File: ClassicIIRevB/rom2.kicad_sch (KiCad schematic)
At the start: 2 parts

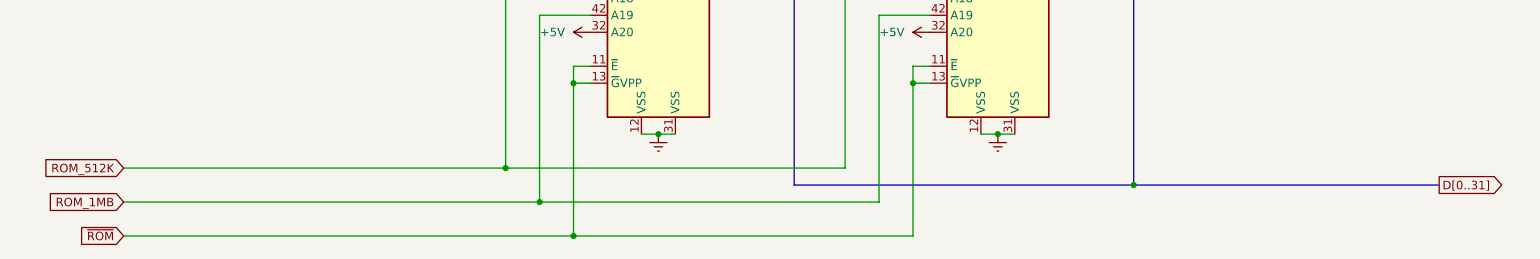
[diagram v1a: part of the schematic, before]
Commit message: Switch to some "official" net names
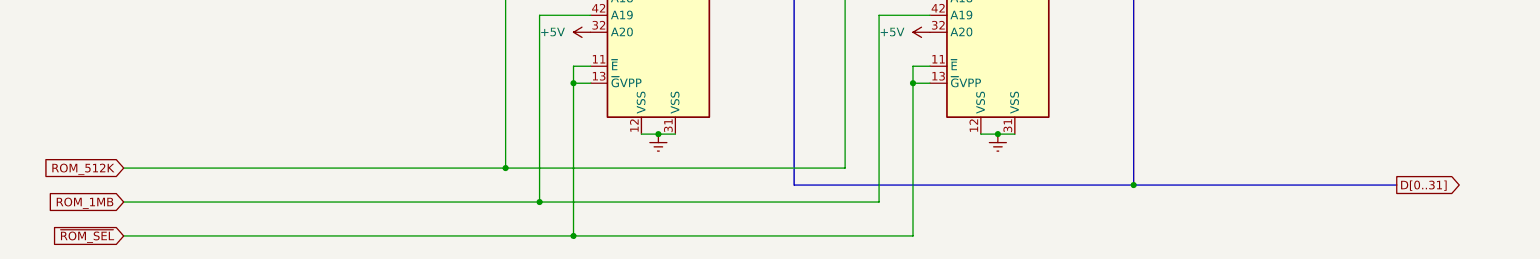
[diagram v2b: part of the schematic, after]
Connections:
- net ~{ROM} renamed ~{ROM_SEL}
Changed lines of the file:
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@@
 	(bus
 		(pts
-			(xy 195.58 139.7) (xy 241.3 139.7)
+			(xy 195.58 139.7) (xy 234.95 139.7)
 		)
 		(stroke
@@
 	(global_label "D[0..31]"
 		(shape output)
-		(at 241.3 139.7 0)
+		(at 234.95 139.7 0)
 		(fields_autoplaced yes)
 		(effects
@@
 		)
 		(property "Intersheetrefs" "${INTERSHEET_REFS}"
-			(at 252.0867 139.7 0)
+			(at 245.7367 139.7 0)
 			(effects
 				(font
@@
 		)
 	)
-	(global_label "~{ROM}"
+	(global_label "~{ROM_SEL}"
 		(shape input)
 		(at 44.45 147.32 180)
@@
 		)
 		(property "Intersheetrefs" "${INTERSHEET_REFS}"
-			(at 34.9334 147.32 0)
+			(at 33.0587 147.32 0)
 			(effects
 				(font

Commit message: update exports
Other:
- title: Macintosh Classic II Revision B -> Macintosh Classic II (Later Revision)
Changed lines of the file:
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@@
 	(paper "USLetter")
 	(title_block
-		(title "Macintosh Classic II Revision B")
-		(date "2025-06-04")
+		(title "Macintosh Classic II (Later Revision)")
+		(date "2025-06-16")
 		(company "Apple Computer")
 		(comment 1 "drawn by Bradley Bell")

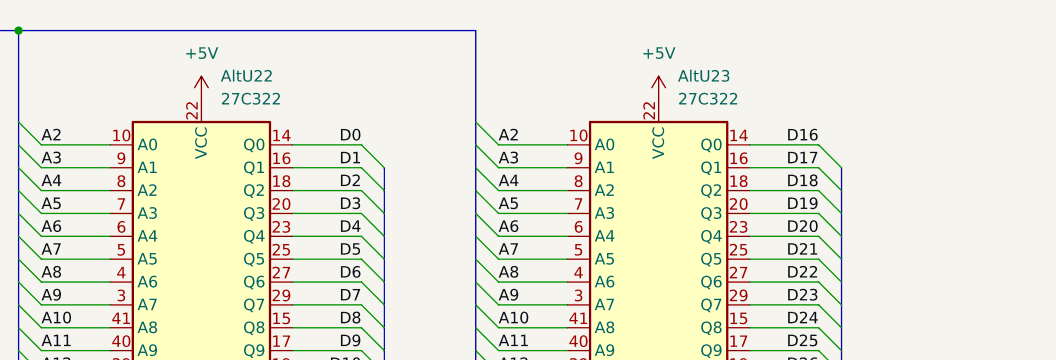
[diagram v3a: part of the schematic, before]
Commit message: Corrections to SMDs, more improved footprints
The later revision board reproduction design is now complete.
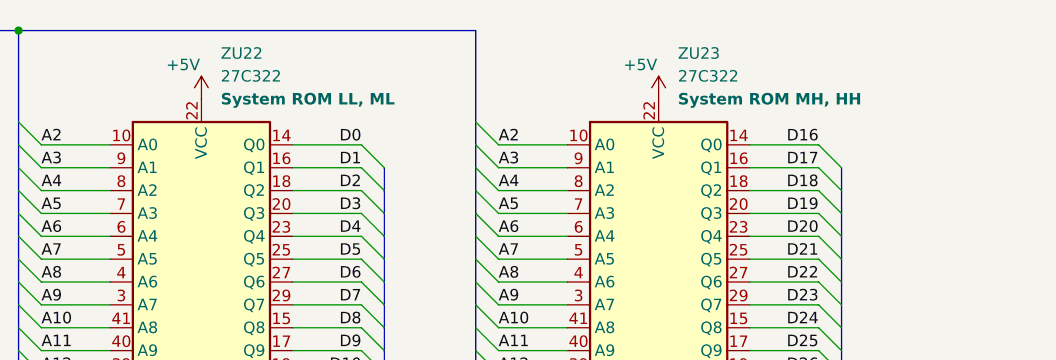
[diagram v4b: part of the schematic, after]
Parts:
- ZU22: renamed from AltU22; footprint Package_DIP:DIP-42_W15.24mm_Socket -> MyPackage:DIP-42_W15.24mm_Socket
- ZU23: renamed from AltU23; footprint Package_DIP:DIP-42_W15.24mm_Socket -> MyPackage:DIP-42_W15.24mm_Socket
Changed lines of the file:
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@@
 	(title_block
 		(title "Macintosh Classic II (Later Revision)")
-		(date "2025-06-16")
+		(date "2025-06-21")
 		(company "Apple Computer")
 		(comment 1 "drawn by Bradley Bell")
@@
 		(on_board yes)
 		(dnp no)
-		(fields_autoplaced yes)
 		(property "Reference" "#PWR0317"
 			(at 175.26 64.77 0)
@@
 		)
 		(property "Value" "+5V"
-			(at 175.26 55.88 0)
+			(at 173.228 57.15 0)
 			(effects
 				(font
@@
 		(dnp no)
 		(fields_autoplaced yes)
-		(property "Reference" "AltU22"
-			(at 126.6033 58.42 0)
+		(property "Reference" "ZU22"
+			(at 126.6033 55.88 0)
 			(effects
 				(font
@@
 		)
 		(property "Value" "27C322"
-			(at 126.6033 60.96 0)
+			(at 126.6033 58.42 0)
 			(effects
 				(font
@@
 			)
 		)
-		(property "Footprint" "Package_DIP:DIP-42_W15.24mm_Socket"
+		(property "Footprint" "MyPackage:DIP-42_W15.24mm_Socket"
 			(at 124.46 93.98 0)
 			(effects
@@
 			)
 		)
-		(property "Description" "OTP EPROM 32 MiBit (2 Megabit x 16)"
-			(at 124.46 93.98 0)
+		(property "Description" "System ROM LL, ML"
+			(at 126.6033 60.96 0)
 			(effects
 				(font
 					(size 1.27 1.27)
+					(thickness 0.254)
+					(bold yes)
 				)
-				(hide yes)
+				(justify left)
 			)
 		)
@@
 			(project "ClassicIIRevB"
 				(path "/08c23af6-72f1-4a8f-a60c-b986fe71300f/51c9cb57-f150-4fef-8266-afe34f9a12a0"
-					(reference "AltU22")
+					(reference "ZU22")
 					(unit 1)
 				)
@@
 		(on_board yes)
 		(dnp no)
-		(fields_autoplaced yes)
 		(property "Reference" "#PWR0314"
 			(at 124.46 64.77 0)
@@
 		)
 		(property "Value" "+5V"
-			(at 124.46 55.88 0)
+			(at 122.428 57.15 0)
 			(effects
 				(font
@@
 		(dnp no)
 		(fields_autoplaced yes)
-		(property "Reference" "AltU23"
-			(at 177.4033 58.42 0)
+		(property "Reference" "ZU23"
+			(at 177.4033 55.88 0)
 			(effects
 				(font
@@
 		)
 		(property "Value" "27C322"
-			(at 177.4033 60.96 0)
+			(at 177.4033 58.42 0)
 			(effects
 				(font
@@
 			)
 		)
-		(property "Footprint" "Package_DIP:DIP-42_W15.24mm_Socket"
+		(property "Footprint" "MyPackage:DIP-42_W15.24mm_Socket"
 			(at 175.26 93.98 0)
 			(effects
@@
 			)
 		)
-		(property "Description" "OTP EPROM 32 MiBit (2 Megabit x 16)"
-			(at 175.26 93.98 0)
+		(property "Description" "System ROM MH, HH"
+			(at 177.4033 60.96 0)
 			(effects
 				(font
 					(size 1.27 1.27)
+					(thickness 0.254)
+					(bold yes)
 				)
-				(hide yes)
+				(justify left)
 			)
 		)
@@
 			(project "ClassicIIRevB"
 				(path "/08c23af6-72f1-4a8f-a60c-b986fe71300f/51c9cb57-f150-4fef-8266-afe34f9a12a0"
-					(reference "AltU23")
+					(reference "ZU23")
 					(unit 1)
 				)
